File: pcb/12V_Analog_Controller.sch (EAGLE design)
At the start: 27 parts, among them J1 POWER, Q1 AO3400, Q2 AO3400, U1 ESP32-PICO-MINI-02, X1 PROG, X2 L1, X3 L2, X5 BOOT, X6 RESET

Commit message: Switch to input power jack
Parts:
- F1, F2: value JK-SMD300L-16 -> JK-SMD300L-24
- J1: device M2M-Connectors:TERMINAL-1X02-5.08 -> M2M-Connectors:XKB-DC-005-5A-2.0
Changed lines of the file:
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@@
 <part name="GND10" library="M2M-Power" deviceset="GND" device=""/>
 <part name="SUPPLY6" library="M2M-Power" deviceset="VCC" device=""/>
-<part name="J1" library="M2M-Connectors" deviceset="TERMINAL-1X02-5.08" device="" value="POWER"/>
+<part name="J1" library="M2M-Connectors" deviceset="XKB-DC-005-5A-2.0" device="" value="POWER"/>
 <part name="SUPPLY2" library="M2M-Power" deviceset="VIN" device=""/>
 <part name="SUPPLY3" library="M2M-Power" deviceset="VIN" device=""/>
@@
 <part name="SUPPLY9" library="M2M-Power" deviceset="VCC" device=""/>
 <part name="SUPPLY10" library="M2M-Power" deviceset="VCC" device=""/>
-<part name="F1" library="M2M-Fuse" deviceset="PTC" device="JK-SMD300" value="JK-SMD300L-16"/>
-<part name="F2" library="M2M-Fuse" deviceset="PTC" device="JK-SMD300" value="JK-SMD300L-16"/>
+<part name="F1" library="M2M-Fuse" deviceset="PTC" device="JK-SMD300" value="JK-SMD300L-24"/>
+<part name="F2" library="M2M-Fuse" deviceset="PTC" device="JK-SMD300" value="JK-SMD300L-24"/>
 <part name="U$3" library="M2M-IC" deviceset="LEGEND-SI-LGS5145" device="" value="LGS5145"/>
 <part name="SUPPLY5" library="M2M-Power" deviceset="VIN" device=""/>
@@
 <attribute name="VALUE" x="165.1" y="155.194" size="1.778" layer="96" align="bottom-center"/>
 </instance>
-<instance part="J1" gate="G$1" x="27.94" y="25.4" smashed="yes" rot="MR0">
-<attribute name="VALUE" x="30.48" y="20.32" size="1.778" layer="96" rot="MR0"/>
-<attribute name="NAME" x="30.48" y="31.242" size="1.778" layer="95" rot="MR0"/>
+<instance part="J1" gate="G$1" x="48.26" y="27.94" smashed="yes" rot="MR0">
+<attribute name="VALUE" x="50.8" y="22.86" size="1.778" layer="96" rot="MR0"/>
+<attribute name="NAME" x="50.8" y="33.782" size="1.778" layer="95" rot="MR0"/>
 </instance>
 <instance part="SUPPLY2" gate="G$1" x="35.56" y="35.56" smashed="yes">
@@
 <segment>
 <pinref part="GND6" gate="1" pin="GND"/>
-<wire x1="33.02" y1="25.4" x2="35.56" y2="25.4" width="0.1524" layer="91"/>
+<wire x1="38.1" y1="25.4" x2="35.56" y2="25.4" width="0.1524" layer="91"/>
 <wire x1="35.56" y1="25.4" x2="35.56" y2="17.78" width="0.1524" layer="91"/>
 <pinref part="J1" gate="G$1" pin="2"/>
@@
 <net name="VIN" class="0">
 <segment>
-<wire x1="33.02" y1="27.94" x2="35.56" y2="27.94" width="0.1524" layer="91"/>
-<wire x1="35.56" y1="27.94" x2="35.56" y2="35.56" width="0.1524" layer="91"/>
+<wire x1="38.1" y1="30.48" x2="35.56" y2="30.48" width="0.1524" layer="91"/>
+<wire x1="35.56" y1="30.48" x2="35.56" y2="35.56" width="0.1524" layer="91"/>
 <pinref part="J1" gate="G$1" pin="1"/>
 <pinref part="SUPPLY2" gate="G$1" pin="VIN"/>

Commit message: Add reverse power protection for internal circuits
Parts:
- added D2: B5819LW, M2M-DiscreteSemi:DIODE-SCHOTTKYSOD-123
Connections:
- new net VSW: D2.A, F1.1, F2.1, J1.1
- net VIN: now also D2.C; no longer F1.1, F2.1, J1.1
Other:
- moved on the sheet: J1
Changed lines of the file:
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@@
 <part name="J1" library="M2M-Connectors" deviceset="XKB-DC-005-5A-2.0" device="" value="POWER"/>
 <part name="SUPPLY2" library="M2M-Power" deviceset="VIN" device=""/>
-<part name="SUPPLY3" library="M2M-Power" deviceset="VIN" device=""/>
-<part name="SUPPLY4" library="M2M-Power" deviceset="VIN" device=""/>
 <part name="R3" library="M2M-Passives" deviceset="RESISTOR" device="0603" value="10K"/>
 <part name="R4" library="M2M-Passives" deviceset="RESISTOR" device="0603" value="10K"/>
@@
 <part name="X2" library="M2M-Connectors" deviceset="XKB-DC-005-5A-2.0" device="" value="L1"/>
 <part name="X3" library="M2M-Connectors" deviceset="XKB-DC-005-5A-2.0" device="" value="L2"/>
+<part name="D2" library="M2M-DiscreteSemi" deviceset="DIODE-SCHOTTKY" device="SOD-123" value="B5819LW"/>
+<part name="SUPPLY8" library="M2M-Power" deviceset="VSW" device=""/>
+<part name="SUPPLY11" library="M2M-Power" deviceset="VSW" device=""/>
+<part name="SUPPLY12" library="M2M-Power" deviceset="VSW" device=""/>
 </parts>
 <sheets>
@@
 <attribute name="VALUE" x="152.4" y="55.626" size="1.778" layer="96" align="top-center"/>
 </instance>
-<instance part="GND6" gate="1" x="35.56" y="15.24" smashed="yes">
-<attribute name="VALUE" x="35.56" y="14.986" size="1.778" layer="96" align="top-center"/>
+<instance part="GND6" gate="1" x="55.88" y="15.24" smashed="yes">
+<attribute name="VALUE" x="55.88" y="14.986" size="1.778" layer="96" align="top-center"/>
 </instance>
 <instance part="X5" gate="G$1" x="43.18" y="55.88" smashed="yes">
@@
 <attribute name="VALUE" x="165.1" y="155.194" size="1.778" layer="96" align="bottom-center"/>
 </instance>
-<instance part="J1" gate="G$1" x="48.26" y="27.94" smashed="yes" rot="MR0">
-<attribute name="VALUE" x="50.8" y="22.86" size="1.778" layer="96" rot="MR0"/>
-<attribute name="NAME" x="50.8" y="33.782" size="1.778" layer="95" rot="MR0"/>
-</instance>
-<instance part="SUPPLY2" gate="G$1" x="35.56" y="35.56" smashed="yes">
-<attribute name="VALUE" x="35.56" y="38.354" size="1.778" layer="96" align="bottom-center"/>
-</instance>
-<instance part="SUPPLY3" gate="G$1" x="195.58" y="152.4" smashed="yes">
-<attribute name="VALUE" x="195.58" y="155.194" size="1.778" layer="96" align="bottom-center"/>
-</instance>
-<instance part="SUPPLY4" gate="G$1" x="195.58" y="96.52" smashed="yes">
-<attribute name="VALUE" x="195.58" y="99.314" size="1.778" layer="96" align="bottom-center"/>
+<instance part="J1" gate="G$1" x="30.48" y="27.94" smashed="yes">
+<attribute name="VALUE" x="27.94" y="22.86" size="1.778" layer="96"/>
+<attribute name="NAME" x="27.94" y="33.782" size="1.778" layer="95"/>
+</instance>
+<instance part="SUPPLY2" gate="G$1" x="55.88" y="35.56" smashed="yes">
+<attribute name="VALUE" x="55.88" y="38.354" size="1.778" layer="96" align="bottom-center"/>
 </instance>
 <instance part="R3" gate="G$1" x="208.28" y="119.38" smashed="yes" rot="R90">
@@
 <attribute name="VALUE" x="30.48" y="132.08" size="1.778" layer="96"/>
 </instance>
-<instance part="SUPPLY5" gate="G$1" x="12.7" y="154.94" smashed="yes">
-<attribute name="VALUE" x="12.7" y="157.734" size="1.778" layer="96" align="bottom-center"/>
+<instance part="SUPPLY5" gate="G$1" x="12.7" y="160.02" smashed="yes">
+<attribute name="VALUE" x="12.7" y="162.814" size="1.778" layer="96" align="bottom-center"/>
 </instance>
 <instance part="GND4" gate="1" x="12.7" y="109.22" smashed="yes">
@@
 <instance part="X2" gate="G$1" x="238.76" y="144.78" smashed="yes" rot="MR0"/>
 <instance part="X3" gate="G$1" x="238.76" y="88.9" smashed="yes" rot="MR0"/>
+<instance part="D2" gate="G$1" x="48.26" y="30.48" smashed="yes" rot="MR180">
+<attribute name="NAME" x="44.45" y="28.702" size="1.778" layer="95" rot="MR180"/>
+<attribute name="VALUE" x="44.45" y="34.036" size="1.778" layer="96" rot="MR180"/>
+</instance>
+<instance part="SUPPLY8" gate="G$1" x="195.58" y="152.4" smashed="yes">
+<attribute name="VALUE" x="195.58" y="155.194" size="1.778" layer="96" align="bottom-center"/>
+</instance>
+<instance part="SUPPLY11" gate="G$1" x="195.58" y="96.52" smashed="yes">
+<attribute name="VALUE" x="195.58" y="99.314" size="1.778" layer="96" align="bottom-center"/>
+</instance>
+<instance part="SUPPLY12" gate="G$1" x="43.18" y="35.56" smashed="yes">
+<attribute name="VALUE" x="43.18" y="38.354" size="1.778" layer="96" align="bottom-center"/>
+</instance>
 </instances>
 <busses>
@@
 <segment>
 <pinref part="GND6" gate="1" pin="GND"/>
-<wire x1="38.1" y1="25.4" x2="35.56" y2="25.4" width="0.1524" layer="91"/>
-<wire x1="35.56" y1="25.4" x2="35.56" y2="17.78" width="0.1524" layer="91"/>
+<wire x1="40.64" y1="25.4" x2="55.88" y2="25.4" width="0.1524" layer="91"/>
+<wire x1="55.88" y1="25.4" x2="55.88" y2="17.78" width="0.1524" layer="91"/>
 <pinref part="J1" gate="G$1" pin="2"/>
 </segment>
@@
 <net name="VIN" class="0">
 <segment>
-<wire x1="38.1" y1="30.48" x2="35.56" y2="30.48" width="0.1524" layer="91"/>
-<wire x1="35.56" y1="30.48" x2="35.56" y2="35.56" width="0.1524" layer="91"/>
-<pinref part="J1" gate="G$1" pin="1"/>
+<wire x1="55.88" y1="30.48" x2="55.88" y2="35.56" width="0.1524" layer="91"/>
 <pinref part="SUPPLY2" gate="G$1" pin="VIN"/>
-</segment>
-<segment>
-<pinref part="SUPPLY3" gate="G$1" pin="VIN"/>
-<pinref part="F1" gate="G$1" pin="1"/>
-<wire x1="195.58" y1="152.4" x2="195.58" y2="147.32" width="0.1524" layer="91"/>
-<wire x1="195.58" y1="147.32" x2="198.12" y2="147.32" width="0.1524" layer="91"/>
-</segment>
-<segment>
-<pinref part="SUPPLY4" gate="G$1" pin="VIN"/>
-<pinref part="F2" gate="G$1" pin="1"/>
-<wire x1="195.58" y1="96.52" x2="195.58" y2="91.44" width="0.1524" layer="91"/>
-<wire x1="195.58" y1="91.44" x2="198.12" y2="91.44" width="0.1524" layer="91"/>
+<pinref part="D2" gate="G$1" pin="C"/>
+<wire x1="50.8" y1="30.48" x2="55.88" y2="30.48" width="0.1524" layer="91"/>
 </segment>
 <segment>
 <pinref part="SUPPLY5" gate="G$1" pin="VIN"/>
 <pinref part="C2" gate="G$1" pin="1"/>
-<wire x1="12.7" y1="154.94" x2="12.7" y2="147.32" width="0.1524" layer="91"/>
+<wire x1="12.7" y1="160.02" x2="12.7" y2="147.32" width="0.1524" layer="91"/>
 <pinref part="U$3" gate="G$1" pin="VIN"/>
 <wire x1="12.7" y1="147.32" x2="12.7" y2="144.78" width="0.1524" layer="91"/>
@@
 </segment>
 </net>
+<net name="VSW" class="0">
+<segment>
+<pinref part="J1" gate="G$1" pin="1"/>
+<pinref part="D2" gate="G$1" pin="A"/>
+<wire x1="40.64" y1="30.48" x2="43.18" y2="30.48" width="0.1524" layer="91"/>
+<pinref part="SUPPLY12" gate="G$1" pin="VSW"/>
+<wire x1="43.18" y1="30.48" x2="45.72" y2="30.48" width="0.1524" layer="91"/>
+<wire x1="43.18" y1="35.56" x2="43.18" y2="30.48" width="0.1524" layer="91"/>
+<junction x="43.18" y="30.48"/>
+</segment>
+<segment>
+<pinref part="F1" gate="G$1" pin="1"/>
+<wire x1="195.58" y1="152.4" x2="195.58" y2="147.32" width="0.1524" layer="91"/>
+<wire x1="195.58" y1="147.32" x2="198.12" y2="147.32" width="0.1524" layer="91"/>
+<pinref part="SUPPLY8" gate="G$1" pin="VSW"/>
+</segment>
+<segment>
+<pinref part="F2" gate="G$1" pin="1"/>
+<wire x1="195.58" y1="96.52" x2="195.58" y2="91.44" width="0.1524" layer="91"/>
+<wire x1="195.58" y1="91.44" x2="198.12" y2="91.44" width="0.1524" layer="91"/>
+<pinref part="SUPPLY11" gate="G$1" pin="VSW"/>
+</segment>
+</net>

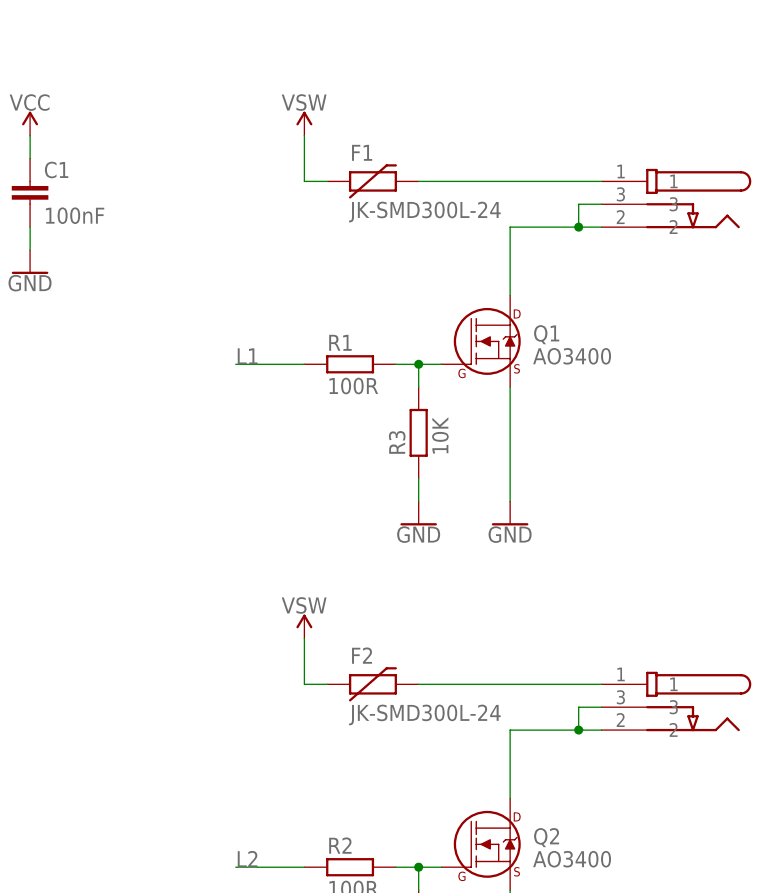
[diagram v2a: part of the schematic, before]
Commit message: Add second PTC footprint
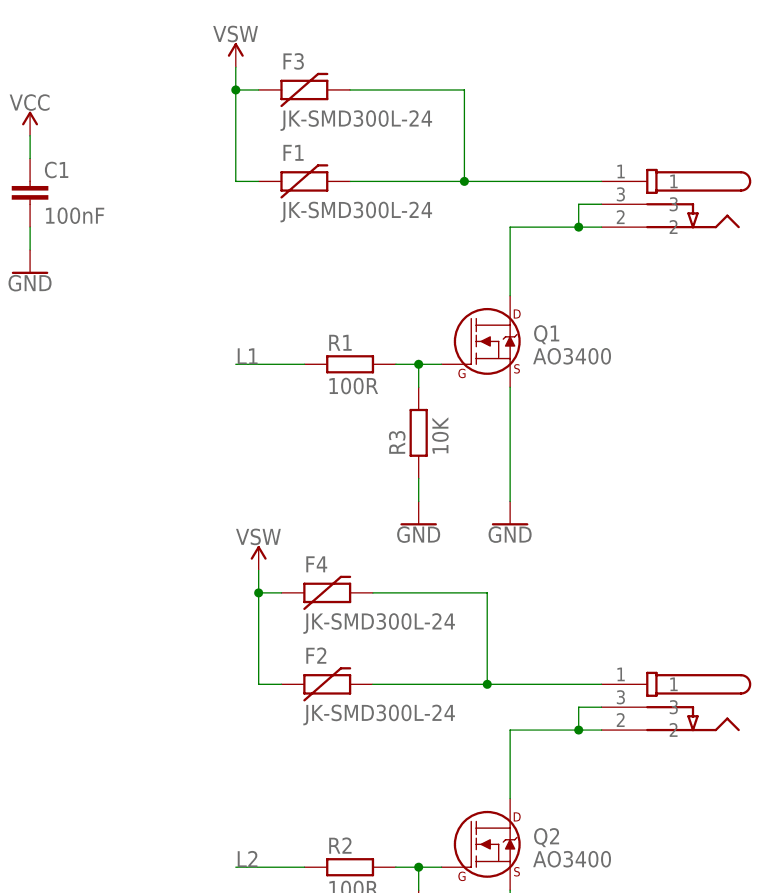
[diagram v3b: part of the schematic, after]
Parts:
- added F3, F4: JK-SMD300L-24, M2M-Fuse:PTCJK-SMD300
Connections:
- net N$5: now also F3.2
- net N$6: now also F4.2
- net VSW: now also F3.1, F4.1
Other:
- moved on the sheet: F1, F2
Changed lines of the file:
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@@
 <part name="SUPPLY11" library="M2M-Power" deviceset="VSW" device=""/>
 <part name="SUPPLY12" library="M2M-Power" deviceset="VSW" device=""/>
+<part name="F3" library="M2M-Fuse" deviceset="PTC" device="JK-SMD300" value="JK-SMD300L-24"/>
+<part name="F4" library="M2M-Fuse" deviceset="PTC" device="JK-SMD300" value="JK-SMD300L-24"/>
 </parts>
 <sheets>
@@
 <attribute name="VALUE" x="66.04" y="76.454" size="1.778" layer="96" align="bottom-center"/>
 </instance>
-<instance part="F1" gate="G$1" x="203.2" y="147.32" smashed="yes">
-<attribute name="NAME" x="200.66" y="149.606" size="1.778" layer="95"/>
-<attribute name="VALUE" x="200.66" y="143.256" size="1.778" layer="95"/>
-</instance>
-<instance part="F2" gate="G$1" x="203.2" y="91.44" smashed="yes">
-<attribute name="NAME" x="200.66" y="93.726" size="1.778" layer="95"/>
-<attribute name="VALUE" x="200.66" y="87.376" size="1.778" layer="95"/>
+<instance part="F1" gate="G$1" x="195.58" y="147.32" smashed="yes">
+<attribute name="NAME" x="193.04" y="149.606" size="1.778" layer="95"/>
+<attribute name="VALUE" x="193.04" y="143.256" size="1.778" layer="95"/>
+</instance>
+<instance part="F2" gate="G$1" x="198.12" y="91.44" smashed="yes">
+<attribute name="NAME" x="195.58" y="93.726" size="1.778" layer="95"/>
+<attribute name="VALUE" x="195.58" y="87.376" size="1.778" layer="95"/>
 </instance>
 <instance part="U$3" gate="G$1" x="38.1" y="142.24" smashed="yes">
@@
 <attribute name="VALUE" x="44.45" y="34.036" size="1.778" layer="96" rot="MR180"/>
 </instance>
-<instance part="SUPPLY8" gate="G$1" x="195.58" y="152.4" smashed="yes">
-<attribute name="VALUE" x="195.58" y="155.194" size="1.778" layer="96" align="bottom-center"/>
-</instance>
-<instance part="SUPPLY11" gate="G$1" x="195.58" y="96.52" smashed="yes">
-<attribute name="VALUE" x="195.58" y="99.314" size="1.778" layer="96" align="bottom-center"/>
+<instance part="SUPPLY8" gate="G$1" x="187.96" y="160.02" smashed="yes">
+<attribute name="VALUE" x="187.96" y="162.814" size="1.778" layer="96" align="bottom-center"/>
+</instance>
+<instance part="SUPPLY11" gate="G$1" x="190.5" y="104.14" smashed="yes">
+<attribute name="VALUE" x="190.5" y="106.934" size="1.778" layer="96" align="bottom-center"/>
 </instance>
 <instance part="SUPPLY12" gate="G$1" x="43.18" y="35.56" smashed="yes">
 <attribute name="VALUE" x="43.18" y="38.354" size="1.778" layer="96" align="bottom-center"/>
+</instance>
+<instance part="F3" gate="G$1" x="195.58" y="157.48" smashed="yes">
+<attribute name="NAME" x="193.04" y="159.766" size="1.778" layer="95"/>
+<attribute name="VALUE" x="193.04" y="153.416" size="1.778" layer="95"/>
+</instance>
+<instance part="F4" gate="G$1" x="198.12" y="101.6" smashed="yes">
+<attribute name="NAME" x="195.58" y="103.886" size="1.778" layer="95"/>
+<attribute name="VALUE" x="195.58" y="97.536" size="1.778" layer="95"/>
 </instance>
 </instances>
@@
 <net name="N$5" class="0">
 <segment>
-<wire x1="228.6" y1="147.32" x2="208.28" y2="147.32" width="0.1524" layer="91"/>
+<wire x1="228.6" y1="147.32" x2="213.36" y2="147.32" width="0.1524" layer="91"/>
 <pinref part="F1" gate="G$1" pin="2"/>
 <pinref part="X2" gate="G$1" pin="1"/>
+<pinref part="F3" gate="G$1" pin="2"/>
+<wire x1="213.36" y1="147.32" x2="200.66" y2="147.32" width="0.1524" layer="91"/>
+<wire x1="200.66" y1="157.48" x2="213.36" y2="157.48" width="0.1524" layer="91"/>
+<wire x1="213.36" y1="157.48" x2="213.36" y2="147.32" width="0.1524" layer="91"/>
+<junction x="213.36" y="147.32"/>
 </segment>
 </net>
 <net name="N$6" class="0">
 <segment>
-<wire x1="228.6" y1="91.44" x2="208.28" y2="91.44" width="0.1524" layer="91"/>
+<wire x1="228.6" y1="91.44" x2="215.9" y2="91.44" width="0.1524" layer="91"/>
 <pinref part="F2" gate="G$1" pin="2"/>
 <pinref part="X3" gate="G$1" pin="1"/>
+<pinref part="F4" gate="G$1" pin="2"/>
+<wire x1="215.9" y1="91.44" x2="203.2" y2="91.44" width="0.1524" layer="91"/>
+<wire x1="203.2" y1="101.6" x2="215.9" y2="101.6" width="0.1524" layer="91"/>
+<wire x1="215.9" y1="101.6" x2="215.9" y2="91.44" width="0.1524" layer="91"/>
+<junction x="215.9" y="91.44"/>
 </segment>
 </net>
@@
 <segment>
 <pinref part="F1" gate="G$1" pin="1"/>
-<wire x1="195.58" y1="152.4" x2="195.58" y2="147.32" width="0.1524" layer="91"/>
-<wire x1="195.58" y1="147.32" x2="198.12" y2="147.32" width="0.1524" layer="91"/>
+<wire x1="187.96" y1="160.02" x2="187.96" y2="157.48" width="0.1524" layer="91"/>
+<wire x1="187.96" y1="157.48" x2="187.96" y2="147.32" width="0.1524" layer="91"/>
+<wire x1="187.96" y1="147.32" x2="190.5" y2="147.32" width="0.1524" layer="91"/>
 <pinref part="SUPPLY8" gate="G$1" pin="VSW"/>
+<pinref part="F3" gate="G$1" pin="1"/>
+<wire x1="190.5" y1="157.48" x2="187.96" y2="157.48" width="0.1524" layer="91"/>
+<junction x="187.96" y="157.48"/>
 </segment>
 <segment>
 <pinref part="F2" gate="G$1" pin="1"/>
-<wire x1="195.58" y1="96.52" x2="195.58" y2="91.44" width="0.1524" layer="91"/>
-<wire x1="195.58" y1="91.44" x2="198.12" y2="91.44" width="0.1524" layer="91"/>
+<wire x1="190.5" y1="104.14" x2="190.5" y2="101.6" width="0.1524" layer="91"/>
+<wire x1="190.5" y1="101.6" x2="190.5" y2="91.44" width="0.1524" layer="91"/>
+<wire x1="190.5" y1="91.44" x2="193.04" y2="91.44" width="0.1524" layer="91"/>
 <pinref part="SUPPLY11" gate="G$1" pin="VSW"/>
-</segment>
-</net>
+<pinref part="F4" gate="G$1" pin="1"/>
+<wire x1="193.04" y1="101.6" x2="190.5" y2="101.6" width="0.1524" layer="91"/>
+<junction x="190.5" y="101.6"/>
+</segment>
+</net>
